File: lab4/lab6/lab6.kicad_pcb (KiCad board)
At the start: 2 copper layers, 10 parts, among them J1 9V, U1 NE555D

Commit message: task 2 pcb
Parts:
- moved C1 29.0 mm to (157.5, 78.7)
- moved R3 28.3 mm to (133.6, 58.4)
- moved J1 27.8 mm to (154.9, 68.6), turned to 90 degrees
- moved R1 24.8 mm to (147.0, 72.5), turned to -90 degrees
- moved D1 24.6 mm to (165.1, 58.4)
- moved D2 14.1 mm to (154.9, 86.4), turned to -90 degrees
- moved U1 12.9 mm to (142.2, 66.0), turned to -90 degrees
- moved R2 7.59 mm to (143.1, 80.2), turned to -90 degrees
- moved C2 4.75 mm to (139.7, 86.3)
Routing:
- net GND: track 0.00 -> 74.3 mm
- net /pin_3: track 0.00 -> 41.5 mm
- net Net-(D1-Pad1): track 0.00 -> 31.8 mm
- net +9V: track 0.00 -> 29.2 mm
- net /pin_2: track 0.00 -> 27.3 mm
- net Net-(D2-Pad2): track 0.00 -> 21.0 mm
- net Net-(C2-Pad1): track 0.00 -> 18.5 mm
- net /pin_7: track 0.00 -> 14.0 mm

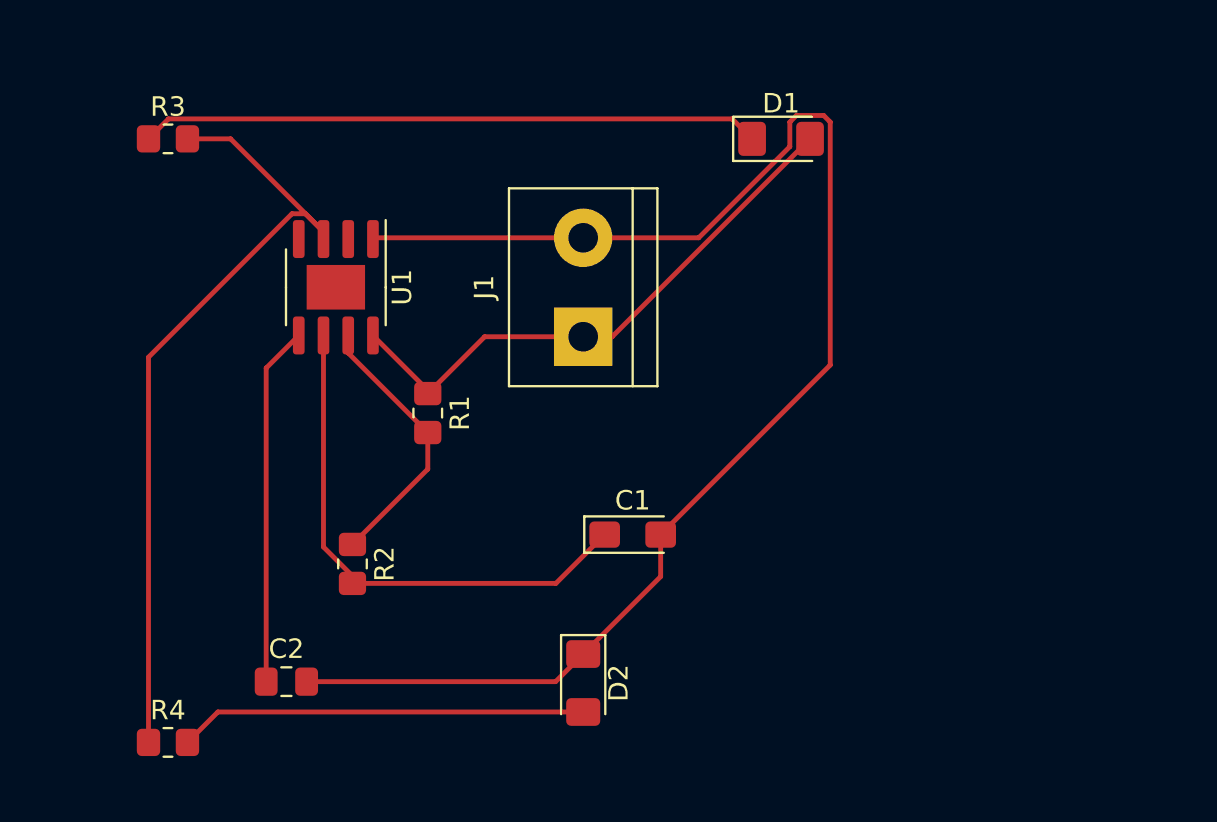
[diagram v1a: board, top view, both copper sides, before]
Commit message: untangled PCB for 555 timer
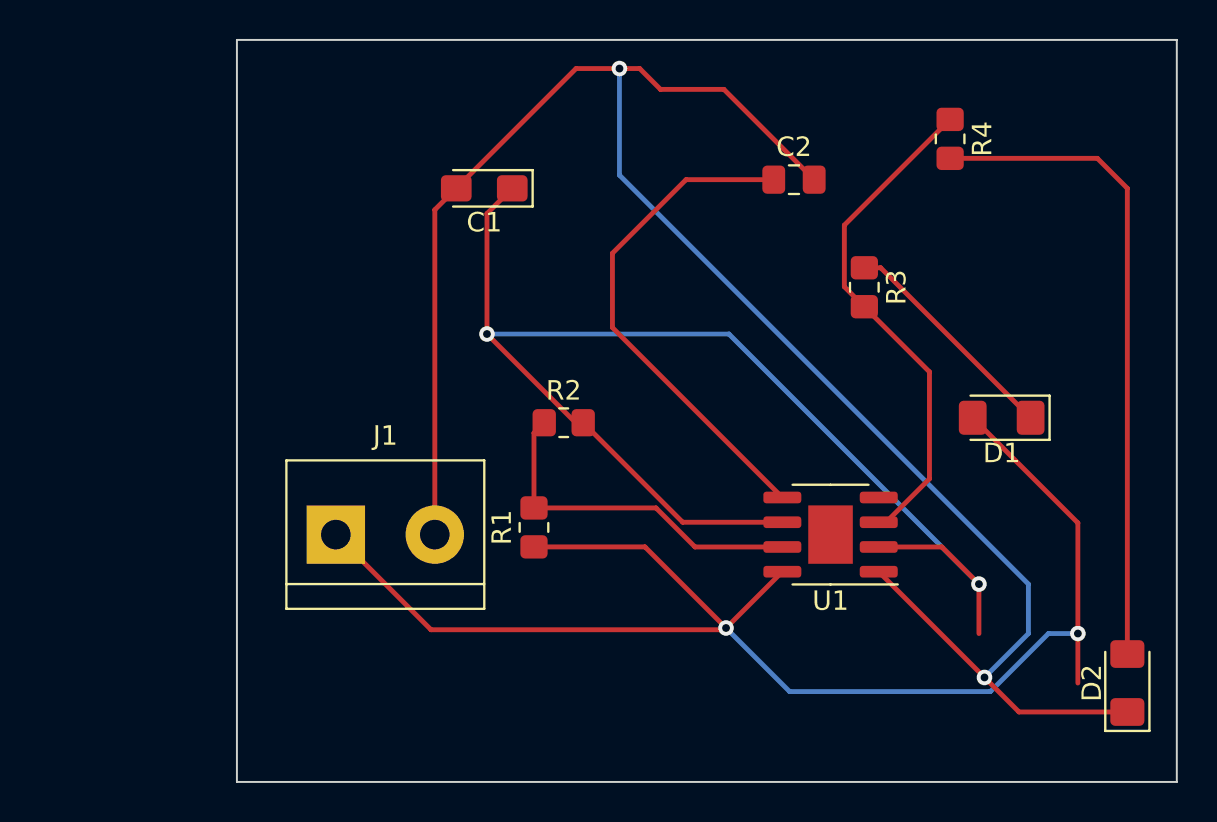
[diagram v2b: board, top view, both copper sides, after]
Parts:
- moved R4 50.7 mm to (173.8, 58.4), turned to -90 degrees
- moved C2 36.7 mm to (165.8, 60.5)
- moved R3 36.6 mm to (169.4, 66.0), turned to -90 degrees
- moved U1 28.4 mm to (167.6, 78.7), turned to 180 degrees
- moved D2 27.9 mm to (182.9, 86.4), turned to 90 degrees
- moved C1 19.3 mm to (149.9, 61.0), turned to 180 degrees
- moved D1 18.3 mm to (176.4, 72.7), turned to 180 degrees
- moved J1 16.3 mm to (142.2, 78.7), turned to 0 degrees
- moved R2 13.0 mm to (153.9, 73.0), turned to 0 degrees
- moved R1 8.01 mm to (152.4, 78.4), turned to 90 degrees
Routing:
- net +9V: track 29.2 -> 74.3 mm, vias 0 -> 2
- net /pin_2: track 27.3 -> 66.2 mm, vias 0 -> 2
- net GND: track 74.3 -> 98.2 mm, vias 0 -> 2
- net Net-(D1-Pad1): track 31.8 -> 11.7 mm
- net /pin_3: track 41.5 -> 26.0 mm
- net Net-(D2-Pad2): track 21.0 -> 33.7 mm
- net Net-(C2-Pad1): track 18.5 -> 26.0 mm
- net /pin_7: track 14.0 -> 18.2 mm
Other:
- board outline added: 48.3 x 38.1 mm
